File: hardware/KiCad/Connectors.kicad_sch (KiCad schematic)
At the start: 23 parts

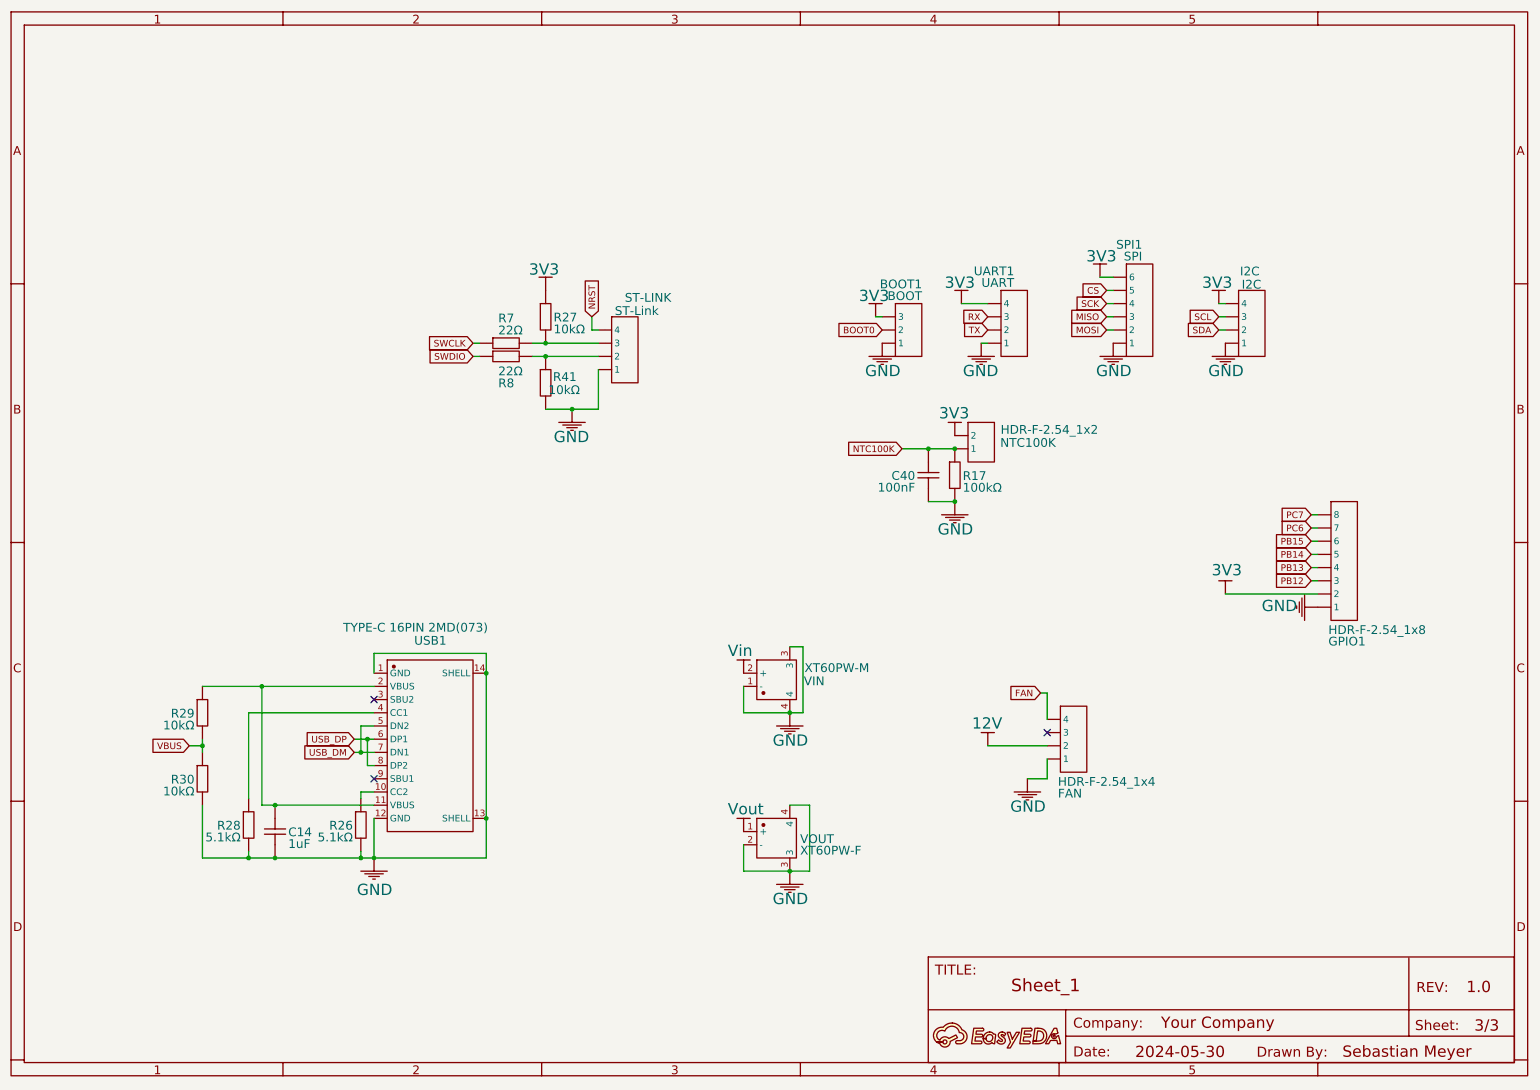
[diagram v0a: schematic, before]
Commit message: added the new 10v regulator
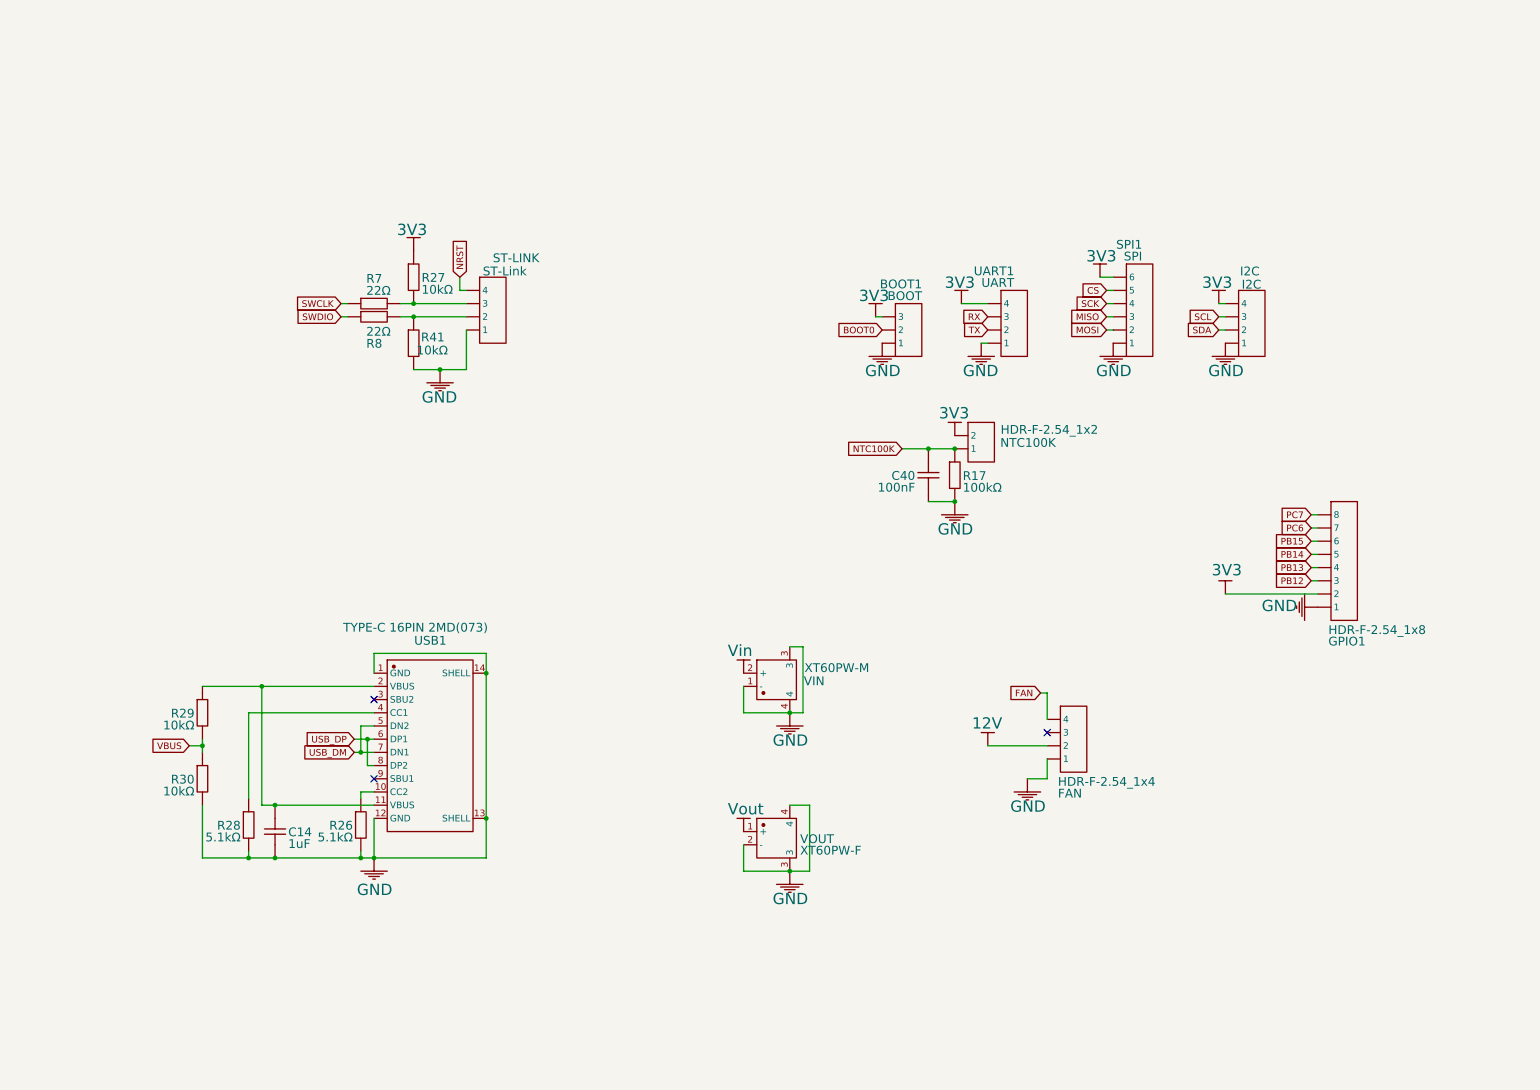
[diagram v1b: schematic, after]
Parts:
- removed A: A, symbol Unknown_0_-806
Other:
- moved on the sheet: R27, R41, R7, R8, ST-LINK

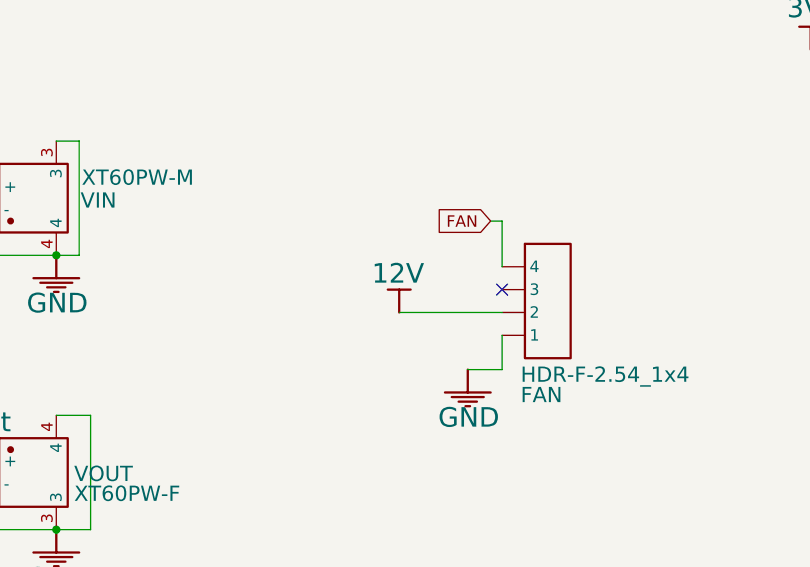
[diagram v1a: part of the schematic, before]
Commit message: added 3v3 regulator
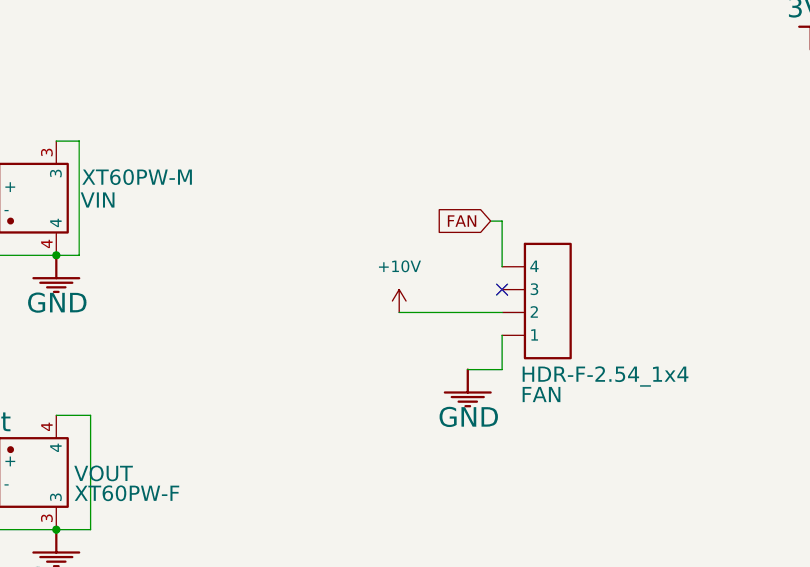
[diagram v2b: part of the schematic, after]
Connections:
- net 12V renamed +10V
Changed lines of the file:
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@@
-	)
-	(symbol
-		(lib_id "12V")
-		(at 187.96 140.97 0)
-		(mirror x)
-		(unit 0)
-		(body_style 0)
-		(exclude_from_sim no)
-		(in_bom yes)
-		(on_board yes)
-		(in_pos_files yes)
-		(dnp no)
-		(property "Reference" "#PWR?"
-			(at 187.96 140.97 0)
-			(hide yes)
-			(show_name no)
-			(do_not_autoplace no)
-			(effects
-				(font
-					(size 1.27 1.27)
-				)
-			)
-		)
-		(property "Value" "12V"
-			(at 184.912 137.922 0)
-			(show_name no)
-			(do_not_autoplace no)
-			(effects
-				(font
-					(face "Times New Roman")
-					(size 2.1717 2.1717)
-				)
-				(justify left top)
-			)
-		)
-		(property "Footprint" ""
-			(at 187.96 140.97 0)
-			(hide yes)
-			(show_name no)
-			(do_not_autoplace no)
-			(effects
-				(font
-					(size 1.27 1.27)
-				)
-			)
-		)
-		(property "Datasheet" ""
-			(at 187.96 140.97 0)
-			(hide yes)
-			(show_name no)
-			(do_not_autoplace no)
-			(effects
-				(font
-					(size 1.27 1.27)
-				)
-			)
-		)
-		(property "Description" "Spannungssymbol erstellt einen globalen Bezeichner mit Namen \"12V\""
-			(at 187.96 140.97 0)
-			(hide yes)
-			(show_name no)
-			(do_not_autoplace no)
-			(effects
-				(font
-					(size 1.27 1.27)
-				)
-			)
-		)
-		(pin "1"
-		)
-		(instances
-			(project "openMPPT_v1.1"
-				(path "/f6f5d1da-a682-42b4-8a9f-7d9a10833a0c/0ca9bfef-bcff-40cb-bb88-2992ce683339"
-					(reference "#PWR?")
-					(unit 0)
-				)
-			)
-		)
 	)
 	(symbol
@@
 				)
 			)
+		)
+	)
+	(symbol
+		(lib_id "power:+10V")
+		(at 187.96 140.97 0)
+		(unit 1)
+		(body_style 1)
+		(exclude_from_sim no)
+		(in_bom yes)
+		(on_board yes)
+		(in_pos_files yes)
+		(dnp no)
+		(fields_autoplaced yes)
+		(property "Reference" "#PWR09"
+			(at 187.96 144.78 0)
+			(hide yes)
+			(show_name no)
+			(do_not_autoplace no)
+			(effects
+				(font
+					(size 1.27 1.27)
+				)
+			)
+		)
+		(property "Value" "+10V"
+			(at 187.96 135.89 0)
+			(show_name no)
+			(do_not_autoplace no)
+			(effects
+				(font
+					(size 1.27 1.27)
+				)
+			)
+		)
+		(property "Footprint" ""
+			(at 187.96 140.97 0)
+			(hide yes)
+			(show_name no)
+			(do_not_autoplace no)
+			(effects
+				(font
+					(size 1.27 1.27)
+				)
+			)
+		)
+		(property "Datasheet" ""
+			(at 187.96 140.97 0)
+			(hide yes)
+			(show_name no)
+			(do_not_autoplace no)
+			(effects
+				(font
+					(size 1.27 1.27)
+				)
+			)
+		)
+		(property "Description" "Power symbol creates a global label with name \"+10V\""
+			(at 187.96 140.97 0)
+			(hide yes)
+			(show_name no)
+			(do_not_autoplace no)
+			(effects
+				(font
+					(size 1.27 1.27)
+				)
+			)
+		)
+		(pin "1"
+		)
+		(instances
+			(project "openMPPT_v1.1"
+				(path "/f6f5d1da-a682-42b4-8a9f-7d9a10833a0c/0ca9bfef-bcff-40cb-bb88-2992ce683339"
+					(reference "#PWR09")
+					(unit 1)
+				)
+			)
